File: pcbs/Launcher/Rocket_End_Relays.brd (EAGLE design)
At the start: 100 x 80 mm, 39 parts, among them IC2 LM2576T-ADJ, K4 LD105, K5 LD105, K6 LD105, K7 LD105, T1 BC547, T2 BC547, T3 BC547, T4 BC547, T5 BC547, U1 ARDUINO-MEGAPRO-5V, X2 22-23-2041, X3 22-23-2021

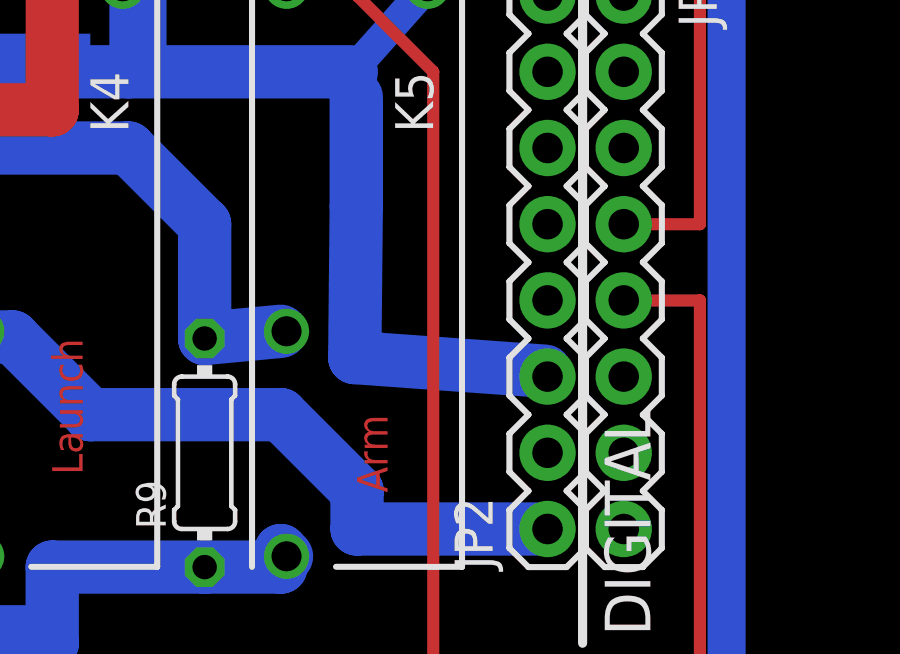
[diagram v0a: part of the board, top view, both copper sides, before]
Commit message: * Put 5volt on pin NEXT to ground.
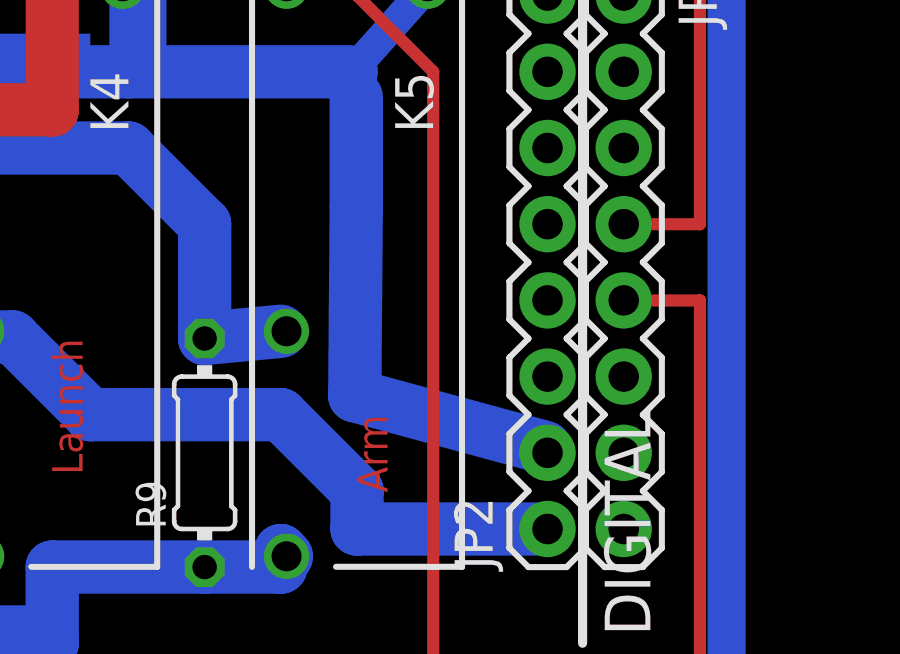
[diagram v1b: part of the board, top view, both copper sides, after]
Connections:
- net N$5: now also JP2.2; no longer JP2.3
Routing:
- net N$5: track 168.6 -> 169.9 mm
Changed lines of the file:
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@@
 <?xml version="1.0" encoding="utf-8"?>
 <!DOCTYPE eagle SYSTEM "eagle.dtd">
-<eagle version="7.1.0">
+<eagle version="7.3.0">
 <drawing>
 <settings>
@@
 <wire x1="22.86" y1="40.64" x2="21.59" y2="39.37" width="1.27" layer="16" curve="90"/>
 <wire x1="24.13" y1="40.64" x2="21.59" y2="38.1" width="1.27" layer="16"/>
-<contactref element="JP2" pad="3"/>
 <wire x1="29.0322" y1="44.8056" x2="29.02" y2="44.76" width="0.254" layer="16"/>
 <wire x1="29.0322" y1="44.8056" x2="29.21" y2="44.45" width="0.254" layer="16"/>
@@
 <wire x1="73.6092" y1="41.8338" x2="73.66" y2="41.91" width="0.254" layer="16"/>
 <wire x1="73.6092" y1="41.3766" x2="73.47" y2="40.95" width="0.254" layer="16"/>
-<wire x1="71.0438" y1="28.575" x2="77.3938" y2="28.1178" width="1.778" layer="16"/>
-<wire x1="71.0946" y1="33.6042" x2="71.0438" y2="28.575" width="1.778" layer="16"/>
+<wire x1="71.0438" y1="27.305" x2="77.3938" y2="25.5778" width="1.778" layer="16"/>
+<wire x1="71.0946" y1="33.6042" x2="71.0438" y2="27.305" width="1.778" layer="16"/>
 <wire x1="71.0946" y1="37.2618" x2="71.0946" y2="33.6042" width="1.778" layer="16"/>
-<wire x1="77.3938" y1="28.1178" x2="77.47" y2="27.94" width="0.254" layer="16"/>
 <wire x1="71.0946" y1="37.2618" x2="70.93" y2="38.1" width="0.254" layer="16"/>
+<contactref element="JP2" pad="2"/>
+<wire x1="77.3938" y1="25.5778" x2="77.47" y2="25.4" width="0" layer="19" extent="16-16"/>
 </signal>
 <signal name="N$32">

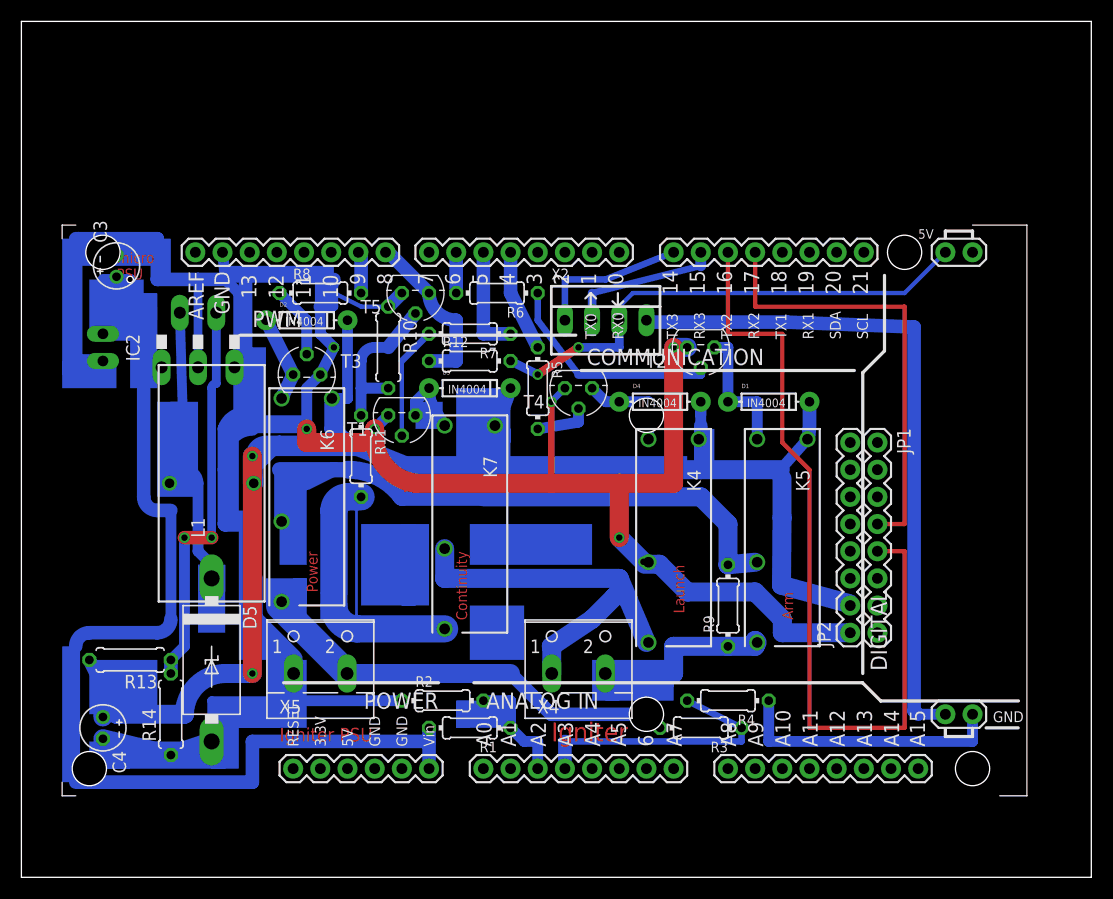
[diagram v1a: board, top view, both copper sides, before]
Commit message: * Correcting the right-angle connector tracks for a RFD900p module connected logo up. Also made sure it was 10mm from the edge of the pdb * Put in correct 2 pin screw terminal blocks with pitch of 3.5mm
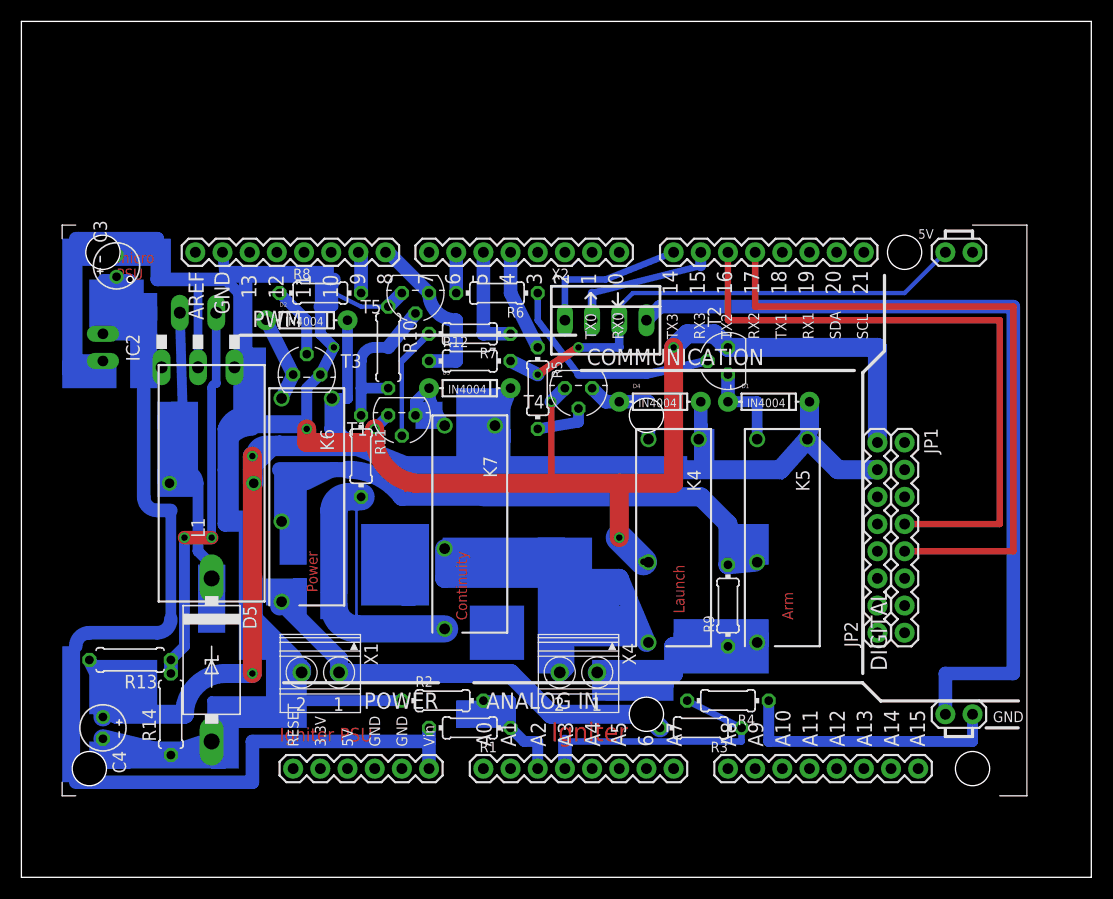
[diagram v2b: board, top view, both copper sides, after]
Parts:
- removed X5: (no value), con-wago-500:W237-102
- added X1: 1751248, con-phoenix-350:1751248
- X4: value (none) -> 1751248; device con-wago-500:W237-102 -> con-phoenix-350:1751248
- moved T2 2.84 mm to (66.0, 48.3), turned to 90 degrees
- moved JP2 2.54 mm to (80.0, 22.9)
- moved JP1 2.54 mm to (82.5, 40.6)
- moved X4 1.27 mm to (52.1, 19.1), turned to 180 degrees
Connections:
- net N$1: now also JP1.4; no longer JP1.5
- net N$15: now also X4.2; no longer X4.1
- net N$17: now also X4.1; no longer X4.2
- net N$2: now also JP1.5; no longer JP1.4
- net N$29: now also X1.1; no longer X5.2
- net N$33: now also JP2.8, X1.2; no longer JP2.1, X5.1
- net N$5: now also JP2.7; no longer JP2.2
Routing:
- net N$2: track 41.9 -> 62.2 mm
- net N$1: track 78.5 -> 59.7 mm
- net N$16: track 64.2 -> 79.7 mm
- net N$5: track 169.9 -> 161.0 mm
- net N$33: track 277.3 -> 282.6 mm
- net N$22: track 12.6 -> 8.77 mm
- net N$15: track 38.5 -> 39.9 mm
- net N$17: track 17.4 -> 18.2 mm
- net N$29: track 40.8 -> 41.5 mm

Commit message: * various updates to pcbs
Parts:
- moved C3 14.0 mm to (7.62, 43.2), turned to 180 degrees
- moved C4 2.54 mm to (10.2, 14.0)
- turned X3 to 0 degrees
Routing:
- net VCC: track 112.1 -> 95.0 mm
- net N$33: track 282.6 -> 271.5 mm
- net N$1: track 59.7 -> 54.6 mm
- net N$2: track 62.2 -> 59.7 mm
- net N$5: track 161.0 -> 162.4 mm
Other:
- board outline removed

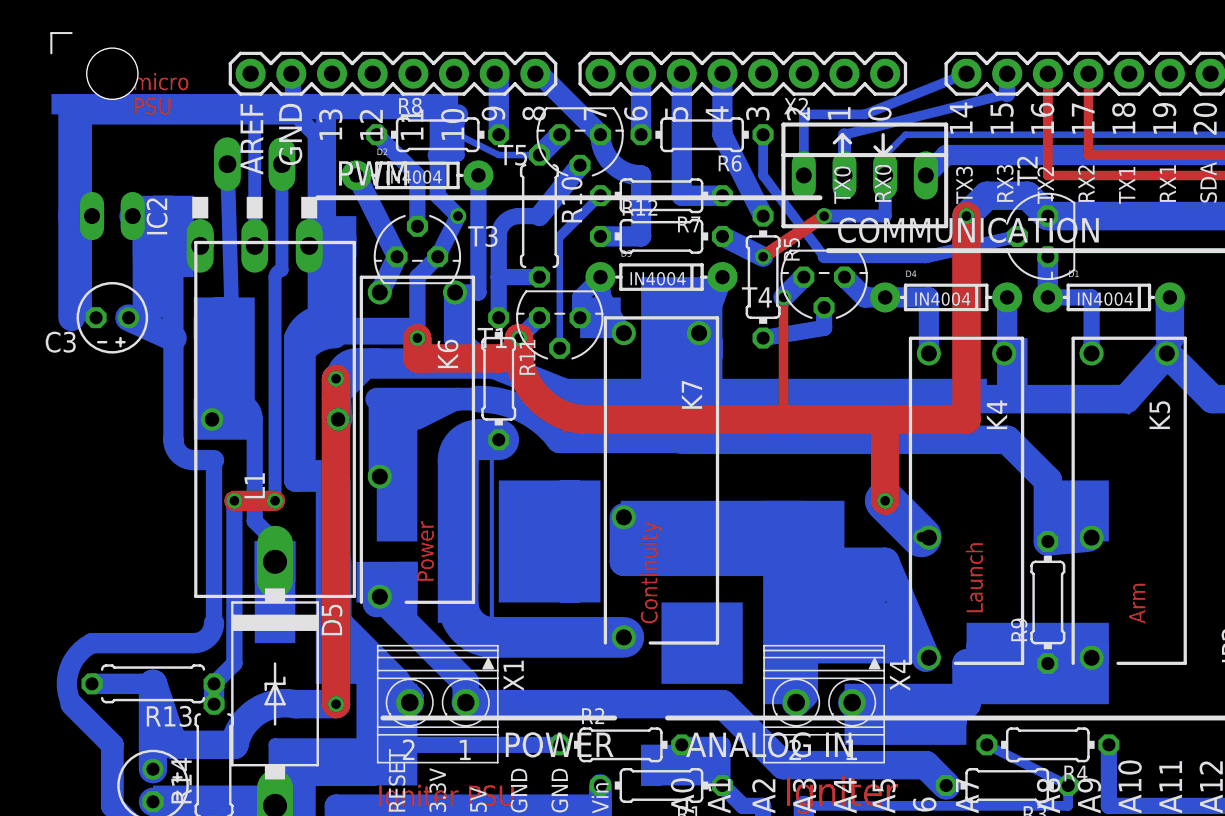
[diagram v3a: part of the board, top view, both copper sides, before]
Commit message: * Widened some tracks * Put 2 x 2-pin connector for 7.4 PSU and Switch.
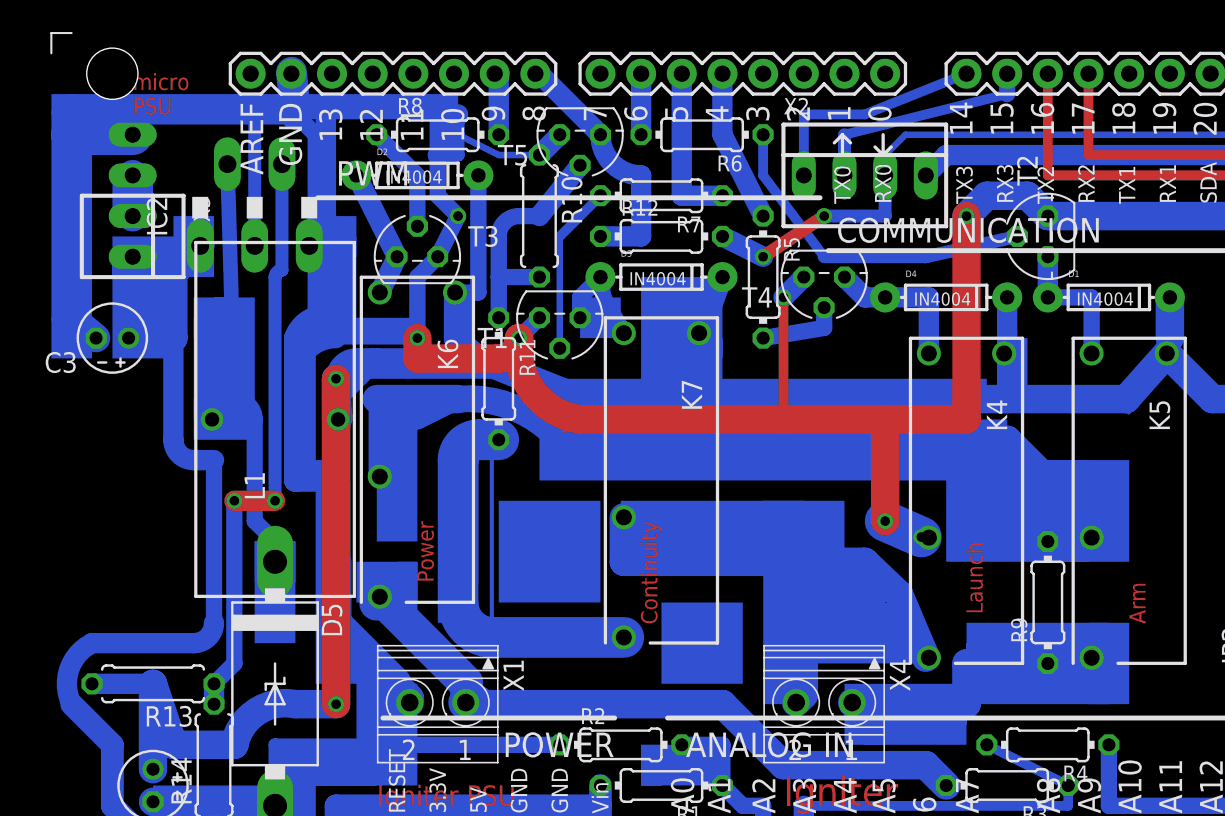
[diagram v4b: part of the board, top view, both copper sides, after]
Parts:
- added X5: 22-23-2021, con-molex:22-23-2021
- moved X3 4.02 mm to (8.89, 53.3), turned to 90 degrees
- moved C3 1.27 mm to (7.62, 41.9)
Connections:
- new net N$18: X3.1, X5.1
- net VCC: now also X5.2; no longer X3.1
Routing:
- net N$33: track 271.5 -> 275.0 mm
- net VCC: track 95.0 -> 92.4 mm
- net N$18: track 0.00 -> 2.54 mm
- net N$15: track 39.9 -> 39.3 mm

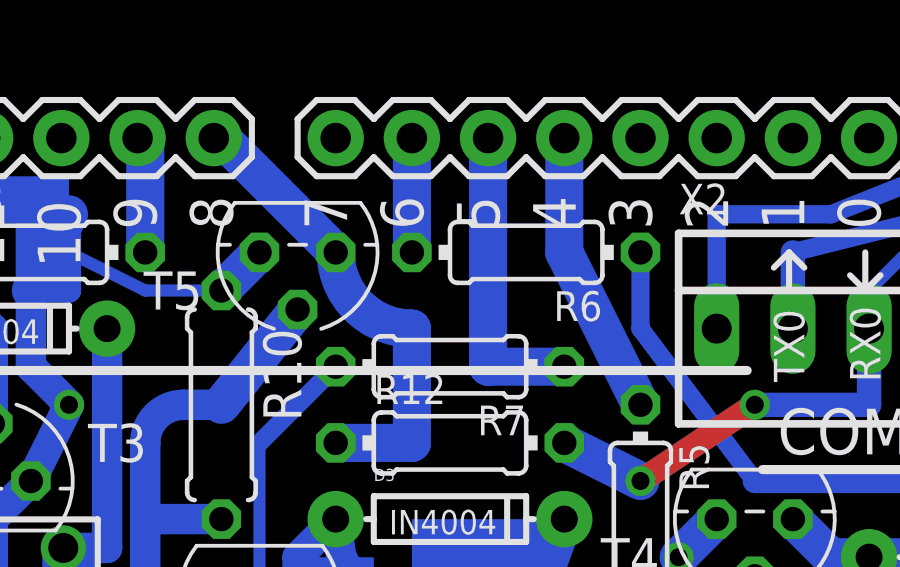
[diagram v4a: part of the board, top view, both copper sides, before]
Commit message: * Moving across pins, so we don't use pin 4. Pin 4 is used by SDCARD CS.
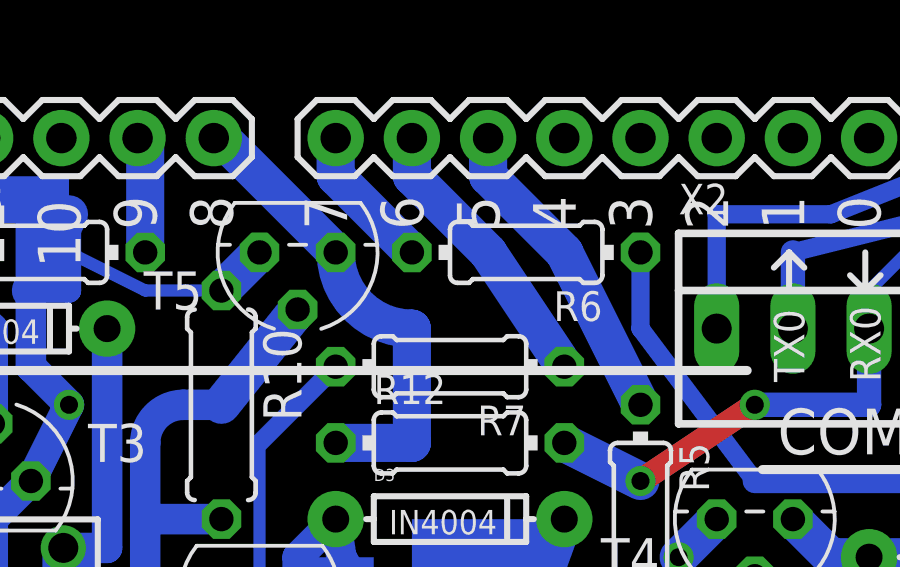
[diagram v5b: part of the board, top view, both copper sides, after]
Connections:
- net N$4: now also U1.5; no longer U1.4
- net N$8: now also U1.6; no longer U1.5
- net N$9: now also U1.7; no longer U1.6
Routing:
- net N$9: track 3.81 -> 4.86 mm
- net N$4: track 9.49 -> 10.5 mm
- net N$8: track 10.2 -> 9.44 mm
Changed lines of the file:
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@@
 </signal>
 <signal name="N$4">
-<contactref element="U1" pad="4"/>
 <contactref element="R5" pad="1"/>
-<wire x1="45.72" y1="58.42" x2="45.72" y2="54.61" width="1.27" layer="16"/>
 <wire x1="45.72" y1="54.61" x2="48.26" y2="49.53" width="1.27" layer="16"/>
-</signal>
-<signal name="N$8">
 <contactref element="U1" pad="5"/>
-<contactref element="R7" pad="1"/>
-<wire x1="45.72" y1="50.8" x2="43.18" y2="50.8" width="1.27" layer="16"/>
-<wire x1="43.18" y1="50.8" x2="43.18" y2="58.42" width="1.27" layer="16"/>
+<wire x1="43.18" y1="58.42" x2="43.18" y2="57.15" width="1.27" layer="16"/>
+<wire x1="43.18" y1="57.15" x2="45.72" y2="54.61" width="1.27" layer="16"/>
 </signal>
 <signal name="N$9">
-<contactref element="U1" pad="6"/>
 <contactref element="R6" pad="2"/>
-<wire x1="40.64" y1="54.61" x2="40.64" y2="58.42" width="1.27" layer="16"/>
+<contactref element="U1" pad="7"/>
+<wire x1="40.64" y1="54.61" x2="38.1" y2="57.15" width="1.27" layer="16"/>
+<wire x1="38.1" y1="57.15" x2="38.1" y2="58.42" width="1.27" layer="16"/>
 </signal>
 <signal name="N$10">
@@
 <wire x1="8.89" y1="52.07" x2="8.89" y2="49.53" width="1.9304" layer="16"/>
 </signal>
+<signal name="N$8">
+<contactref element="R7" pad="1"/>
+<contactref element="U1" pad="6"/>
+<wire x1="45.72" y1="50.8" x2="43.18" y2="54.61" width="1.27" layer="16"/>
+<wire x1="43.18" y1="54.61" x2="40.64" y2="57.15" width="1.27" layer="16"/>
+<wire x1="40.64" y1="57.15" x2="40.64" y2="58.42" width="1.27" layer="16"/>
+</signal>
 </signals>
